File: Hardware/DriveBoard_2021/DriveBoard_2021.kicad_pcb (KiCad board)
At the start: 2 copper layers, 87 parts, among them SW1 SW_Push, SW2 SW_Push, SW3 SW_Push, SW4 SW_Push, SW5 SW_Push, SW6 SW_Push, SW7 SW_Push, U1 LM2576S-3.3, U2 LM2576HVS-5, U3 TM4C129E_Launchpad, U4 MCP2551-I-SN

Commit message: Odrive Pads Updated, Board Outline Finished, Andersons added to board
12VA pin on anderson symbol was re-assigned to work on pad 2 for 2 port anderson connector.
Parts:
- added LED25: green, LED_SMD:LED_0603_1608Metric_Pad1.05x0.95mm_HandSolder, F.Cu at (193.2, -5.30)
- added R26: 1K, Resistor_SMD:R_0603_1608Metric_Pad1.05x0.95mm_HandSolder, F.Cu at (193.2, -2.75)
- Conn1: footprint MRDT_Connectors:Anderson_2_Horizontal_Side_by_Side -> MRDT_Connectors:Anderson_3_Horizontal_Side_by_Side
- moved BL_WHL2 146.5 mm to (90.2, 65.5)
- moved F2 139.5 mm to (362.1, 115.7)
- moved LED24 139.5 mm to (361.3, 154.8)
- moved R17 139.5 mm to (356.8, 162.4)
- moved R21 139.5 mm to (365.6, 157.3)
- moved R22 139.5 mm to (369.4, 151.5)
- moved R23 139.5 mm to (373.7, 149.0)
- moved R24 139.5 mm to (356.8, 164.9)
- moved R7 139.5 mm to (369.4, 149.0)
- moved R8 139.5 mm to (356.8, 159.9)
- moved R9 139.5 mm to (361.2, 157.3)
- moved SW1 139.5 mm to (386.1, 135.1)
- moved LED1 139.5 mm to (363.5, 117.8)
- moved LED13 139.5 mm to (356.9, 154.8)
- moved LED14 139.5 mm to (356.9, 157.4)
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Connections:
- C1 pad 1: +12VA -> +12V
- C2 pad 1: +12VA -> +12V
- Conn1 pad 2: (no net) -> +12V
- Conn2 pad 2: (no net) -> Net-(Conn2-Pad2)
- Conn3 pad 2: (no net) -> Net-(Conn3-Pad2)
- F1 pad 2: Net-(Conn2-Pad3) -> Net-(Conn2-Pad2)
- F2 pad 1: Net-(Conn2-Pad3) -> Net-(Conn2-Pad2)
- F2 pad 2: Net-(Conn3-Pad3) -> Net-(Conn3-Pad2)
- U1 pad 1: +12VA -> +12V
- U2 pad 1: +12VA -> +12V
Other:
- board outline added: 124.5 x 101.6 mm

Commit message: Fixed pad issue for PWR in. Added bucks to board.
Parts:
- moved SW1 287.0 mm to (100.1, 111.3)
- moved U4 267.8 mm to (120.7, 81.0)
- moved F2 262.5 mm to (99.8, 105.2)
- moved F1 199.7 mm to (99.8, 96.5)
- moved D1 141.8 mm to (160.8, 108.5), turned to 90 degrees
- moved SW2 141.1 mm to (111.5, 111.3)
- moved D2 116.0 mm to (127.0, 108.5), turned to 90 degrees
- moved U1 13.8 mm to (150.3, 100.5)
- moved U2 13.6 mm to (137.4, 100.5)
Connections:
- Conn1 pad 3: (no net) -> +12VA
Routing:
- net RT_TURN: track 0.00 -> 2.18 mm, vias 0 -> 1
- net LT_TURN: track 0.00 -> 2.05 mm, vias 0 -> 1
- net FR_DRIVE: track 0.00 -> 2.05 mm, vias 0 -> 1
- net FL_DRIVE: track 0.00 -> 2.05 mm, vias 0 -> 1
- net BR_DRIVE: track 0.00 -> 2.05 mm, vias 0 -> 1
- net BL_DRIVE: track 0.00 -> 2.05 mm, vias 0 -> 1
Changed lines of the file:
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@@
     (thickness 1.6)
     (drawings 24)
-    (tracks 0)
+    (tracks 25)
     (zones 0)
     (modules 89)
@@
   )
   (setup
-    (last_trace_width 0.25)
+    (last_trace_width 0.254)
+    (user_trace_width 0.254)
+    (user_trace_width 0.381)
     (trace_clearance 0.2)
     (zone_clearance 0.508)
@@
     (pad 2 thru_hole circle (at 3.556 -11.811 180) (size 5.08 5.08) (drill 4.06) (layers *.Cu *.Mask F.Paste)
       (net 111 +12V))
-    (pad 3 thru_hole circle (at 3.556 -3.937 180) (size 5.08 5.08) (drill 4.06) (layers *.Cu *.Mask F.Paste))
+    (pad 3 thru_hole circle (at 3.556 -3.937 180) (size 5.08 5.08) (drill 4.06) (layers *.Cu *.Mask F.Paste)
+      (net 11 +12VA))
     (model "${MRDT_KICAD_LIBRARIES}/3D Files/MRDT_Connctors/Anderson_3_Horizontal_Side_by_Side.stp"
       (offset (xyz 0 0 7.619999885559082))
@@
   )
   (module Package_SO:SOIC-8_3.9x4.9mm_P1.27mm (layer F.Cu)
-    (at 386.669 111.66)
+    (at 120.65 81.026)
     (descr "SOIC, 8 Pin (JEDEC MS-012AA, https://www.analog.com/media/en/package-pcb-resources/package/pkg_pdf/soic_narrow-r/r_8.pdf), generated with kicad-footprint-generator ipc_gullwing_generator.py")
     (tags "SOIC SO")
@@
   )
   (module Package_TO_SOT_SMD:TO-263-5_TabPin3 (layer F.Cu)
-    (at 150.622 103.632 90)
+    (at 137.395 100.542 90)
     (descr "TO-263 / D2PAK / DDPAK SMD package, http://www.infineon.com/cms/en/product/packages/PG-TO263/PG-TO263-5-1/")
     (tags "D2PAK DDPAK TO-263 D2PAK-5 TO-263-5 SOT-426")
@@
   )
   (module Package_TO_SOT_SMD:TO-263-5_TabPin3 (layer F.Cu)
-    (at 136.906 103.632 90)
+    (at 150.349 100.542 90)
     (descr "TO-263 / D2PAK / DDPAK SMD package, http://www.infineon.com/cms/en/product/packages/PG-TO263/PG-TO263-5-1/")
     (tags "D2PAK DDPAK TO-263 D2PAK-5 TO-263-5 SOT-426")
@@
   )
   (module Button_Switch_SMD:SW_SPST_TL3305A (layer F.Cu)
-    (at 130.353 251.038)
+    (at 111.506 111.252)
     (descr https://www.e-switch.com/system/asset/product_line/data_sheet/213/TL3305.pdf)
     (tags "TL3305 Series Tact Switch")
@@
   )
   (module Button_Switch_SMD:SW_SPST_TL3305A (layer F.Cu)
-    (at 386.059 135.13)
+    (at 100.076 111.252)
     (descr https://www.e-switch.com/system/asset/product_line/data_sheet/213/TL3305.pdf)
     (tags "TL3305 Series Tact Switch")
@@
   )
   (module MRDT_Passives:ATC_Fuse_Block (layer F.Cu)
-    (at 362.063999 115.741)
+    (at 99.822 105.156)
     (tags "Fuse ATC")
     (fp_text reference F2 (at 1.905 1.27) (layer Dwgs.User) hide
@@
   )
   (module MRDT_Passives:ATC_Fuse_Block (layer F.Cu)
-    (at 298.737999 79.217)
+    (at 99.822 96.52)
     (tags "Fuse ATC")
     (fp_text reference F1 (at 1.905 1.27) (layer Dwgs.User) hide
@@
   )
   (module Diode_THT:D_DO-201AD_P15.24mm_Horizontal (layer F.Cu)
-    (at 108.219 222.888)
+    (at 127 108.458 90)
     (descr "Diode, DO-201AD series, Axial, Horizontal, pin pitch=15.24mm, , length*diameter=9.5*5.2mm^2, , http://www.diodes.com/_files/packages/DO-201AD.pdf")
     (tags "Diode DO-201AD series Axial Horizontal pin pitch 15.24mm  length 9.5mm diameter 5.2mm")
-    (fp_text reference D2 (at 7.62 -3.72) (layer F.SilkS)
+    (fp_text reference D2 (at 7.62 -3.72 90) (layer F.SilkS)
       (effects (font (size 1 1) (thickness 0.15)))
     )
-    (fp_text value 1N5822 (at 7.62 3.72) (layer F.Fab)
+    (fp_text value 1N5822 (at 7.62 3.72 90) (layer F.Fab)
       (effects (font (size 1 1) (thickness 0.15)))
     )
-    (fp_text user K (at 0 -2.6) (layer F.SilkS)
+    (fp_text user K (at 0 -2.6 90) (layer F.SilkS)
       (effects (font (size 1 1) (thickness 0.15)))
     )
-    (fp_text user K (at 0 -2.6) (layer F.Fab)
+    (fp_text user K (at 0 -2.6 90) (layer F.Fab)
       (effects (font (size 1 1) (thickness 0.15)))
     )
-    (fp_text user %R (at 8.3325 0) (layer F.Fab)
+    (fp_text user %R (at 8.3325 0 90) (layer F.Fab)
       (effects (font (size 1 1) (thickness 0.15)))
     )
@@
     (fp_line (start 2.87 2.6) (end 12.37 2.6) (layer F.Fab) (width 0.1))
     (fp_line (start 2.87 -2.6) (end 2.87 2.6) (layer F.Fab) (width 0.1))
-    (pad 2 thru_hole oval (at 15.24 0) (size 3.2 3.2) (drill 1.6) (layers *.Cu *.Mask)
+    (pad 2 thru_hole oval (at 15.24 0 90) (size 3.2 3.2) (drill 1.6) (layers *.Cu *.Mask)
       (net 2 GND))
-    (pad 1 thru_hole rect (at 0 0) (size 3.2 3.2) (drill 1.6) (layers *.Cu *.Mask)
+    (pad 1 thru_hole rect (at 0 0 90) (size 3.2 3.2) (drill 1.6) (layers *.Cu *.Mask)
       (net 17 "Net-(D2-Pad1)"))
     (model ${KISYS3DMOD}/Diode_THT.3dshapes/D_DO-201AD_P15.24mm_Horizontal.wrl
@@
   )
   (module Diode_THT:D_DO-201AD_P15.24mm_Horizontal (layer F.Cu)
-    (at 300.363 83.336)
+    (at 160.782 108.458 90)
     (descr "Diode, DO-201AD series, Axial, Horizontal, pin pitch=15.24mm, , length*diameter=9.5*5.2mm^2, , http://www.diodes.com/_files/packages/DO-201AD.pdf")
     (tags "Diode DO-201AD series Axial Horizontal pin pitch 15.24mm  length 9.5mm diameter 5.2mm")
-    (fp_text reference D1 (at 7.62 -3.72) (layer F.SilkS)
+    (fp_text reference D1 (at 7.62 -3.72 90) (layer F.SilkS)
       (effects (font (size 1 1) (thickness 0.15)))
     )
-    (fp_text value 1N5822 (at 7.62 3.72) (layer F.Fab)
+    (fp_text value 1N5822 (at 7.62 3.72 90) (layer F.Fab)
       (effects (font (size 1 1) (thickness 0.15)))
     )
-    (fp_text user K (at 0 -2.6) (layer F.SilkS)
+    (fp_text user K (at 0 -2.6 90) (layer F.SilkS)
       (effects (font (size 1 1) (thickness 0.15)))
     )
-    (fp_text user K (at 0 -2.6) (layer F.Fab)
+    (fp_text user K (at 0 -2.6 90) (layer F.Fab)
       (effects (font (size 1 1) (thickness 0.15)))
     )
-    (fp_text user %R (at 8.3325 0) (layer F.Fab)
+    (fp_text user %R (at 8.3325 0 90) (layer F.Fab)
       (effects (font (size 1 1) (thickness 0.15)))
     )
@@
     (fp_line (start 2.87 2.6) (end 12.37 2.6) (layer F.Fab) (width 0.1))
     (fp_line (start 2.87 -2.6) (end 2.87 2.6) (layer F.Fab) (width 0.1))
-    (pad 2 thru_hole oval (at 15.24 0) (size 3.2 3.2) (drill 1.6) (layers *.Cu *.Mask)
+    (pad 2 thru_hole oval (at 15.24 0 90) (size 3.2 3.2) (drill 1.6) (layers *.Cu *.Mask)
       (net 2 GND))
-    (pad 1 thru_hole rect (at 0 0) (size 3.2 3.2) (drill 1.6) (layers *.Cu *.Mask)
+    (pad 1 thru_hole rect (at 0 0 90) (size 3.2 3.2) (drill 1.6) (layers *.Cu *.Mask)
       (net 16 "Net-(D1-Pad1)"))
     (model ${KISYS3DMOD}/Diode_THT.3dshapes/D_DO-201AD_P15.24mm_Horizontal.wrl
@@
   (gr_line (start 194.31 104.902) (end 194.31 71.374) (layer Edge.Cuts) (width 0.249936))
   (gr_line (start 69.85 137.922) (end 69.85 71.374) (layer Edge.Cuts) (width 0.249936))
+  (segment (start 81.317 84.5244) (end 81.317 85.6674) (width 0.254) (layer B.Cu) (net 46))
+  (segment (start 81.317 85.6674) (end 81.317 86.577) (width 0.254) (layer B.Cu) (net 46))
+  (segment (start 81.317 86.577) (end 81.317 86.577) (width 0.254) (layer B.Cu) (net 46))
+  (via (at 81.317 86.577) (size 0.8) (drill 0.4) (layers F.Cu B.Cu) (net 46))
+  (segment (start 83.857 84.5244) (end 83.857 85.6674) (width 0.254) (layer B.Cu) (net 47))
+  (segment (start 83.857 85.6674) (end 83.857 86.577) (width 0.254) (layer B.Cu) (net 47))
+  (segment (start 83.857 86.577) (end 83.857 86.577) (width 0.254) (layer B.Cu) (net 47))
+  (via (at 83.857 86.577) (size 0.8) (drill 0.4) (layers F.Cu B.Cu) (net 47))
+  (segment (start 86.397 84.5244) (end 86.397 85.6674) (width 0.254) (layer B.Cu) (net 48))
+  (segment (start 86.397 85.6674) (end 86.397 86.45) (width 0.254) (layer B.Cu) (net 48))
+  (segment (start 86.397 86.45) (end 86.397 86.577) (width 0.254) (layer B.Cu) (net 48))
+  (segment (start 86.397 86.577) (end 86.397 86.577) (width 0.254) (layer B.Cu) (net 48))
+  (via (at 86.397 86.577) (size 0.8) (drill 0.4) (layers F.Cu B.Cu) (net 48))
+  (segment (start 88.937 84.5244) (end 88.937 85.6674) (width 0.254) (layer B.Cu) (net 49))
+  (segment (start 88.937 85.6674) (end 88.937 86.577) (width 0.254) (layer B.Cu) (net 49))
+  (segment (start 88.937 86.577) (end 88.937 86.577) (width 0.254) (layer B.Cu) (net 49))
+  (via (at 88.937 86.577) (size 0.8) (drill 0.4) (layers F.Cu B.Cu) (net 49))
+  (segment (start 91.477 84.5244) (end 91.477 85.6674) (width 0.254) (layer B.Cu) (net 50))
+  (segment (start 91.477 85.6674) (end 91.477 86.577) (width 0.254) (layer B.Cu) (net 50))
+  (segment (start 91.477 86.577) (end 91.477 86.577) (width 0.254) (layer B.Cu) (net 50))
+  (via (at 91.477 86.577) (size 0.8) (drill 0.4) (layers F.Cu B.Cu) (net 50))
+  (segment (start 94.017 84.5244) (end 94.017 85.6674) (width 0.254) (layer B.Cu) (net 51))
+  (segment (start 94.017 85.6674) (end 94.017 86.704) (width 0.254) (layer B.Cu) (net 51))
+  (segment (start 94.017 86.704) (end 94.017 86.704) (width 0.254) (layer B.Cu) (net 51))
+  (via (at 94.017 86.704) (size 0.8) (drill 0.4) (layers F.Cu B.Cu) (net 51))
 )

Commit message: All Major Components footprints placed.
Remaining are resistors, capacitors, and inductors. Silkscreen is also required.
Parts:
- moved SW7 171.1 mm to (108.7, 91.9)
- moved SW4 168.7 mm to (95.0, 91.9)
- moved C6 164.9 mm to (134.1, 111.9), turned to 270 degrees
- moved C4 162.7 mm to (166.4, 98.0)
- moved C1 161.0 mm to (129.0, 111.9), turned to 270 degrees
- moved SW3 158.0 mm to (95.0, 99.8)
- moved C5 156.3 mm to (147.1, 111.6), turned to 270 degrees
- moved C2 154.9 mm to (142.0, 111.6), turned to 270 degrees
- moved C3 153.3 mm to (166.4, 101.6)
- moved SW5 152.7 mm to (108.7, 107.7)
- moved SW6 151.6 mm to (108.7, 99.8)
- moved F2 73.4 mm to (167.1, 75.9), turned to 270 degrees
- moved F1 66.8 mm to (166.6, 95.8), turned to 90 degrees
- moved SW2 16.9 mm to (95.0, 107.7)
- moved Conn3 7.41 mm to (180.8, 88.9)
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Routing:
- net +12V: track 0.00 -> 66.1 mm
- net GND: track 0.00 -> 47.1 mm, vias 0 -> 4
- net FL_DRIVE: track 2.05 -> 40.5 mm
- net LT_TURN: track 2.05 -> 35.2 mm
- net FR_DRIVE: track 2.05 -> 30.3 mm
- net Net-(Conn2-Pad2): track 0.00 -> 27.2 mm
- net DIR_SWITCH: track 0.00 -> 26.3 mm, vias 0 -> 1
- net RT_TURN: track 2.18 -> 25.2 mm
- net +12VA: track 0.00 -> 22.8 mm
- net BL_DRIVE: track 2.05 -> 20.4 mm
- net Net-(D1-Pad1): track 0.00 -> 15.4 mm
- net Net-(D2-Pad1): track 0.00 -> 15.2 mm
- net BR_DRIVE: track 2.05 -> 10.7 mm
- net Net-(Conn3-Pad2): track 0.00 -> 8.59 mm
- net +5V: track 0.00 -> 5.00 mm

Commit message: Added traces for buttons, and moved most resistors and LEDs into position
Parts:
- moved LED5 263.0 mm to (100.6, 125.1), turned to 90 degrees
- moved R7 261.9 mm to (109.0, 121.0), turned to 90 degrees
- moved LED6 260.2 mm to (103.4, 125.1), turned to 90 degrees
- moved LED14 244.5 mm to (114.6, 125.0), turned to 90 degrees
- moved R4 204.4 mm to (100.6, 121.0), turned to 90 degrees
- moved R1 202.5 mm to (164.8, 110.1), turned to 270 degrees
- moved LED1 198.7 mm to (164.8, 114.7), turned to 90 degrees
- moved R6 174.8 mm to (106.2, 121.0), turned to 90 degrees
- moved R5 174.0 mm to (103.4, 121.0), turned to 90 degrees
- moved R13 165.5 mm to (114.6, 121.0), turned to 90 degrees
- moved R14 164.2 mm to (117.3, 121.0), turned to 90 degrees
- moved R15 163.2 mm to (120.1, 121.0), turned to 90 degrees
- moved L2 161.8 mm to (131.6, 111.9), turned to 90 degrees
- moved R2 161.0 mm to (139.2, 110.6), turned to 270 degrees
- moved R3 160.1 mm to (137.2, 110.6), turned to 270 degrees
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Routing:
- net BR_DRIVE: track 10.7 -> 44.1 mm
- net DIR_SWITCH: track 26.3 -> 56.2 mm
- net BL_DRIVE: track 20.4 -> 43.6 mm
- net RT_TURN: track 25.2 -> 46.8 mm
- net +12V: track 66.1 -> 79.9 mm
- net FR_DRIVE: track 30.3 -> 43.9 mm
- net LT_TURN: track 35.2 -> 47.7 mm
- net GND: track 47.1 -> 56.3 mm, vias 4 -> 5
- net +5V: track 5.00 -> 12.1 mm
- net Net-(D2-Pad1): track 15.2 -> 20.4 mm
- net FL_DRIVE: track 40.5 -> 45.0 mm
- net +12VA: track 22.8 -> 27.1 mm
- net Net-(LED1-Pad2): track 0.00 -> 3.45 mm
- net Net-(LED25-Pad2): track 0.00 -> 2.71 mm
- net Net-(LED7-Pad2): track 0.00 -> 2.31 mm
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
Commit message: All Components in Place. Small amounts of trace work remaining.
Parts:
- moved R23 302.4 mm to (73.0, 117.1), turned to 180 degrees
- moved R21 285.7 mm to (82.7, 117.1), turned to 180 degrees
- moved LED24 285.5 mm to (77.9, 119.9), turned to 180 degrees
- moved R22 284.0 mm to (87.5, 117.1), turned to 180 degrees
- moved R24 283.1 mm to (77.8, 117.1), turned to 180 degrees
- moved R9 282.3 mm to (92.7, 70.2), turned to 270 degrees
- moved R8 281.3 mm to (90.2, 70.2), turned to 270 degrees
- moved R17 270.2 mm to (102.9, 70.2), turned to 270 degrees
- moved LED13 252.1 mm to (118.1, 73.8), turned to 90 degrees
- moved R11 226.3 mm to (80.0, 70.2), turned to 270 degrees
- moved R18 206.6 mm to (105.4, 70.2), turned to 270 degrees
- moved R12 203.6 mm to (115.6, 70.2), turned to 270 degrees
- moved LED4 202.7 mm to (90.2, 73.8), turned to 90 degrees
- moved LED12 193.4 mm to (115.6, 73.8), turned to 90 degrees
- moved R16 193.2 mm to (118.1, 70.2), turned to 270 degrees
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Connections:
- C3 pad 2: Net-(C3-Pad2) -> GND
- C4 pad 2: Net-(C3-Pad2) -> GND
- Conn1 pad 1: Net-(C3-Pad2) -> GND
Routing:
- net GND: track 56.3 -> 160.9 mm, vias 5 -> 12
- net BR_PWM: track 0.00 -> 98.2 mm
- net BL_PWM: track 0.00 -> 88.1 mm
- net FR_PWM: track 0.00 -> 77.7 mm
- net FL_PWM: track 0.00 -> 67.8 mm
- net CANL: track 0.00 -> 63.6 mm, vias 0 -> 1
- net CANH: track 0.00 -> 62.2 mm
- net OD2_Tx: track 0.00 -> 41.7 mm, vias 0 -> 1
- net OD2_Rx: track 0.00 -> 33.9 mm, vias 0 -> 1
- net +5V: track 12.1 -> 38.2 mm, vias 0 -> 2
- net OD1_Rx: track 0.00 -> 25.6 mm, vias 0 -> 1
- net OD1_Tx: track 0.00 -> 25.5 mm, vias 0 -> 1
- net RT_TURN: track 46.8 -> 54.0 mm
- net LT_TURN: track 47.7 -> 54.9 mm
- net FR_DRIVE: track 43.9 -> 51.1 mm
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- added copper zone on F.Cu, net +3V3
- added copper zone on B.Cu, net GND

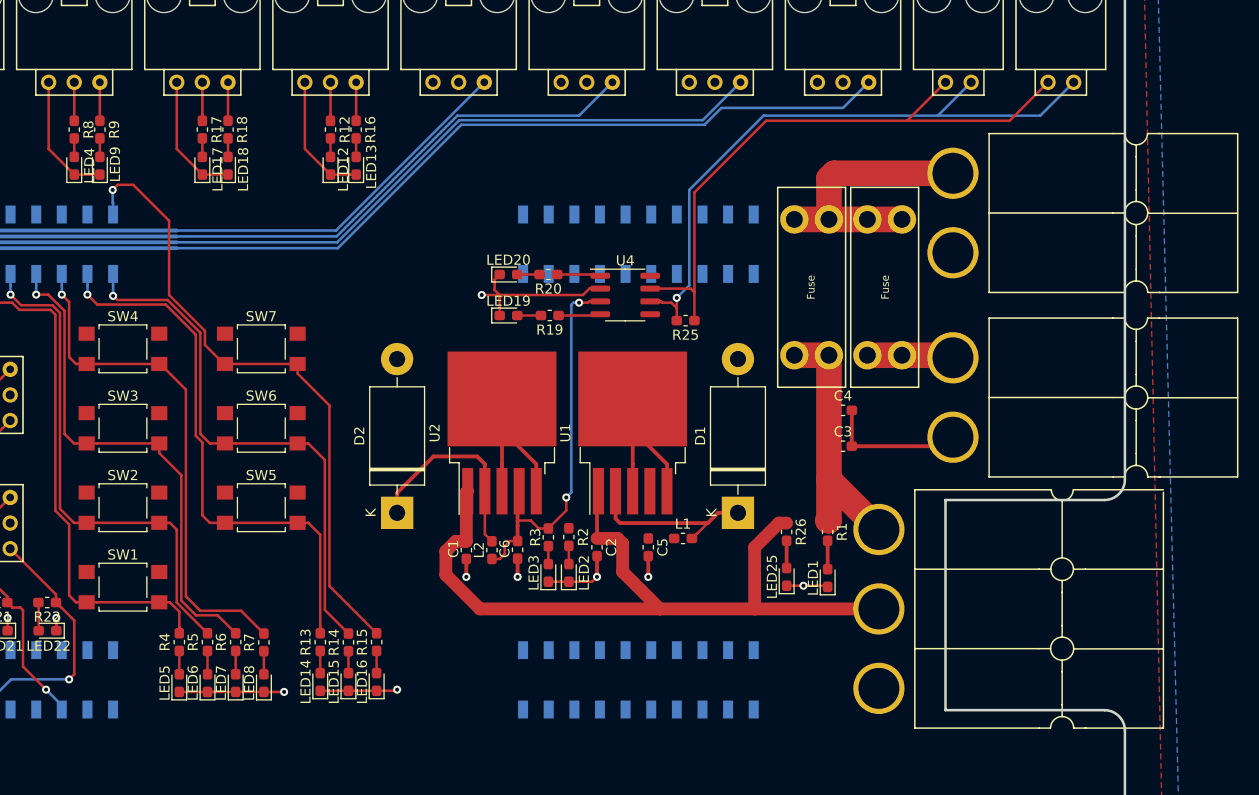
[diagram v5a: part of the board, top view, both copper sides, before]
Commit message: Adjusted Power Footprints and made Andersons flush with edge of board
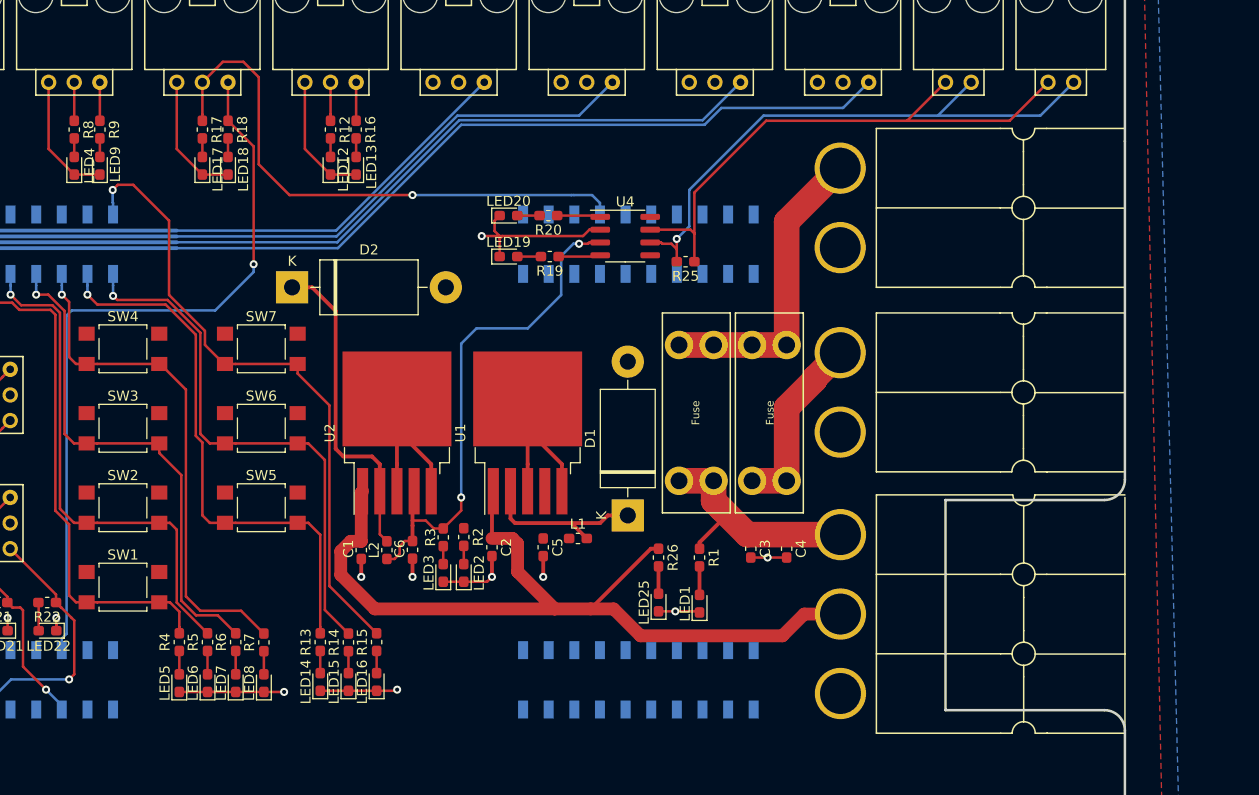
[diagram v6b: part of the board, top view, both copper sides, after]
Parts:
- moved D2 24.7 mm to (111.8, 85.9), turned to 0 degrees
- moved F1 16.9 mm to (155.2, 108.2)
- moved F2 16.9 mm to (155.7, 88.4)
- moved C4 14.8 mm to (160.8, 111.8), turned to 270 degrees
- moved C3 13.7 mm to (157.2, 111.8), turned to 270 degrees
- moved R1 13.0 mm to (152.1, 112.6)
- moved R26 13.0 mm to (148.1, 112.6)
- moved LED1 13.0 mm to (152.1, 117.2)
- moved LED25 13.0 mm to (148.1, 117.1)
- moved Conn2 11.2 mm to (169.7, 70.1)
- moved Conn3 11.2 mm to (169.7, 88.4)
- moved D1 10.9 mm to (145.0, 108.5)
- moved C1 10.4 mm to (118.6, 111.9)
- moved C5 10.4 mm to (136.7, 111.6)
- moved LED2 10.4 mm to (128.8, 114.2)
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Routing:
- net FL_Rx: track 3.81 -> 73.5 mm, vias 0 -> 1
- net FL_Tx: track 3.81 -> 56.1 mm, vias 0 -> 1
- net +5V: track 38.2 -> 51.4 mm
- net Net-(D2-Pad1): track 20.4 -> 31.9 mm
- net GND: track 160.9 -> 150.5 mm, vias 12 -> 13
- net Net-(Conn3-Pad2): track 8.59 -> 18.3 mm
- net +12V: track 79.9 -> 87.4 mm
- net CANL: track 63.6 -> 57.7 mm
- net CANH: track 62.2 -> 56.4 mm
- net Net-(Conn2-Pad2): track 27.2 -> 30.4 mm
- net +12VA: track 27.1 -> 24.2 mm
- net Net-(D1-Pad1): track 17.7 -> 17.0 mm
